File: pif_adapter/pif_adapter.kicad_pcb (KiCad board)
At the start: 2 copper layers, 11 x 21.5 mm, 11 parts, among them P1 Conn_02x20_Odd_Even, P10 Conn_01x01, P11 Conn_01x01, P2 PIF-NUS, P3 Conn_01x01, P4 Conn_01x01, P5 Conn_01x01, P6 Conn_01x01, P7 Conn_01x01, P8 Conn_01x01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

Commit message: routing changes
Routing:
- net GND: track 51.7 -> 50.4 mm
- net +3V3: track 14.6 -> 15.2 mm

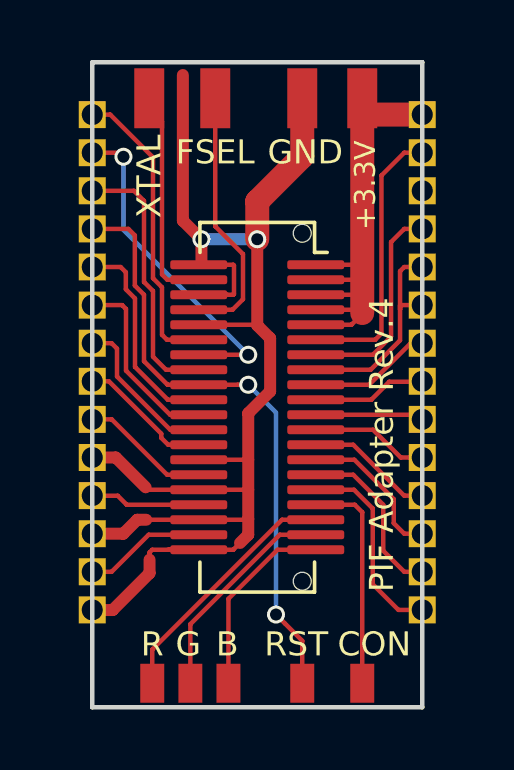
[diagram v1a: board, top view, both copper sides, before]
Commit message: changed the PCB-edges for manual via cutting
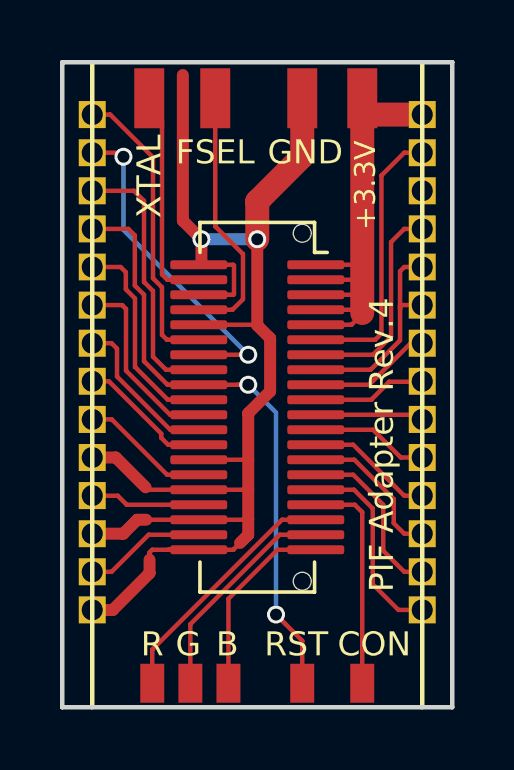
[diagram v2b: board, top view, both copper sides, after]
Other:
- board size 11 x 21.5 mm -> 13 x 21.5 mm
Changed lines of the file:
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@@
   (general
     (thickness 1.6)
-    (drawings 20)
+    (drawings 22)
     (tracks 203)
     (zones 0)
@@
     (38 B.Mask user hide)
     (39 F.Mask user hide)
-    (40 Dwgs.User user)
+    (40 Dwgs.User user hide)
     (41 Cmts.User user)
     (42 Eco1.User user)
@@
     (pad_to_mask_clearance 0.15)
     (solder_mask_min_width 0.3)
-    (aux_axis_origin 141 95.5)
+    (aux_axis_origin 140 95.5)
     (visible_elements 7FFFFFFF)
     (pcbplotparams
@@
       (net 28 /RED))
   )
+  (gr_line (start 152 95.5) (end 152 117) (layer F.SilkS) (width 0.15))
+  (gr_line (start 141 95.5) (end 141 117) (layer F.SilkS) (width 0.15))
   (gr_text RST (at 147.8 114.9) (layer F.SilkS)
     (effects (font (size 0.8 0.8) (thickness 0.15)))
@@
     (effects (font (size 0.8 0.8) (thickness 0.15)))
   )
-  (gr_line (start 152 117) (end 152 95.5) (layer Edge.Cuts) (width 0.15))
-  (gr_line (start 141 117) (end 152 117) (layer Edge.Cuts) (width 0.15))
+  (gr_line (start 153 117) (end 153 95.5) (layer Edge.Cuts) (width 0.15))
+  (gr_line (start 140 117) (end 153 117) (layer Edge.Cuts) (width 0.15))
   (dimension 21.5 (width 0.3) (layer Dwgs.User)
     (gr_text "21,500 mm" (at 136.9 106.25 270) (layer Dwgs.User)
@@
     (arrow2b (pts (xy 140 94) (xy 141.126504 93.413579)))
   )
-  (gr_line (start 141 95.5) (end 141 117) (layer Edge.Cuts) (width 0.15))
-  (gr_line (start 141 95.5) (end 152 95.5) (layer Edge.Cuts) (width 0.15))
+  (gr_line (start 140 95.5) (end 140 117) (layer Edge.Cuts) (width 0.15))
+  (gr_line (start 140 95.5) (end 153 95.5) (layer Edge.Cuts) (width 0.15))
   (segment (start 141.6 97.245) (end 141 97.245) (width 0.15) (layer F.Cu) (net 1))
   (segment (start 143.49 104.75) (end 143.325 104.585) (width 0.15) (layer F.Cu) (net 1))
